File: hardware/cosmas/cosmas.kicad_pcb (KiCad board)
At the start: 2 copper layers, 23 parts, among them J1 12V DC, J2 I2C_LCD_SCREEN, J3 MOTORA, J4 MOTORB, J5 DRIVER-POWER, J6 MOTOR-CONTROL, J7 MOT_A, J8 MOT_A, SW1 ON/OFF, U2 AMS1117-3.3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

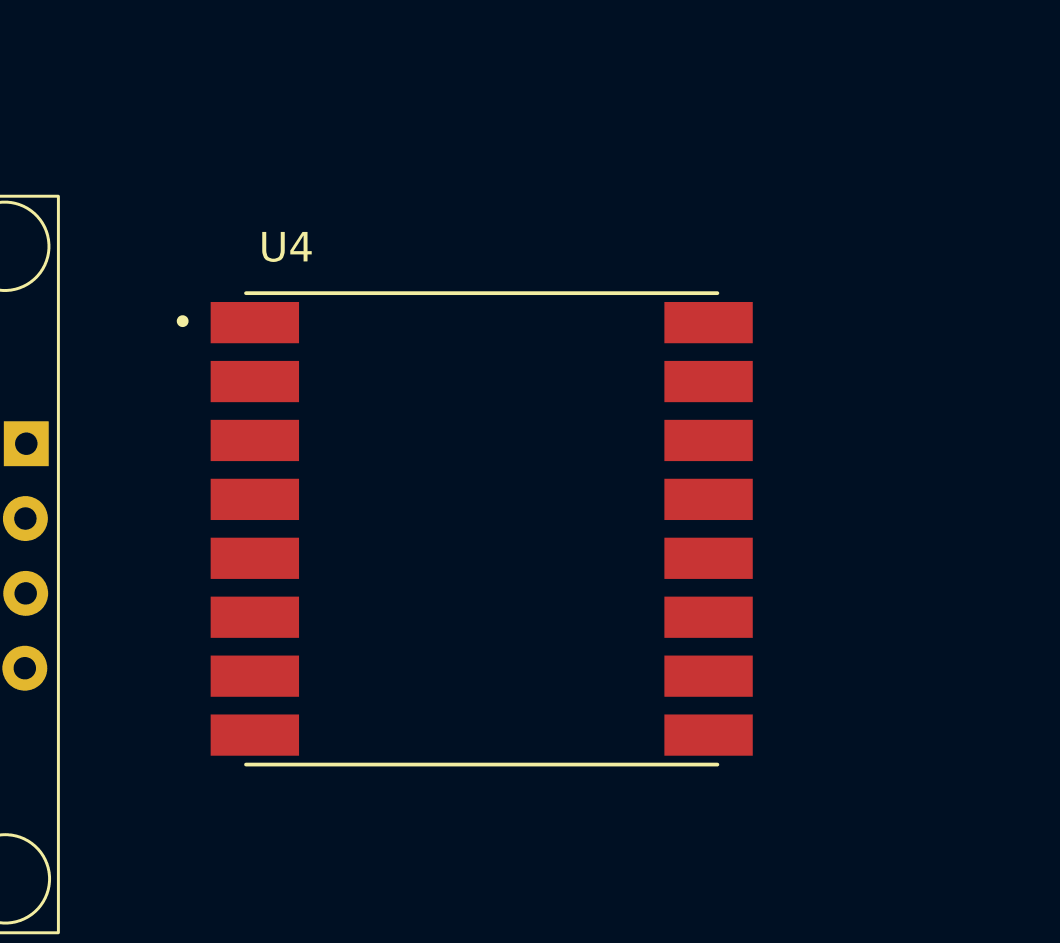
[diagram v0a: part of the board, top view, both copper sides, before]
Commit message: updates net labels
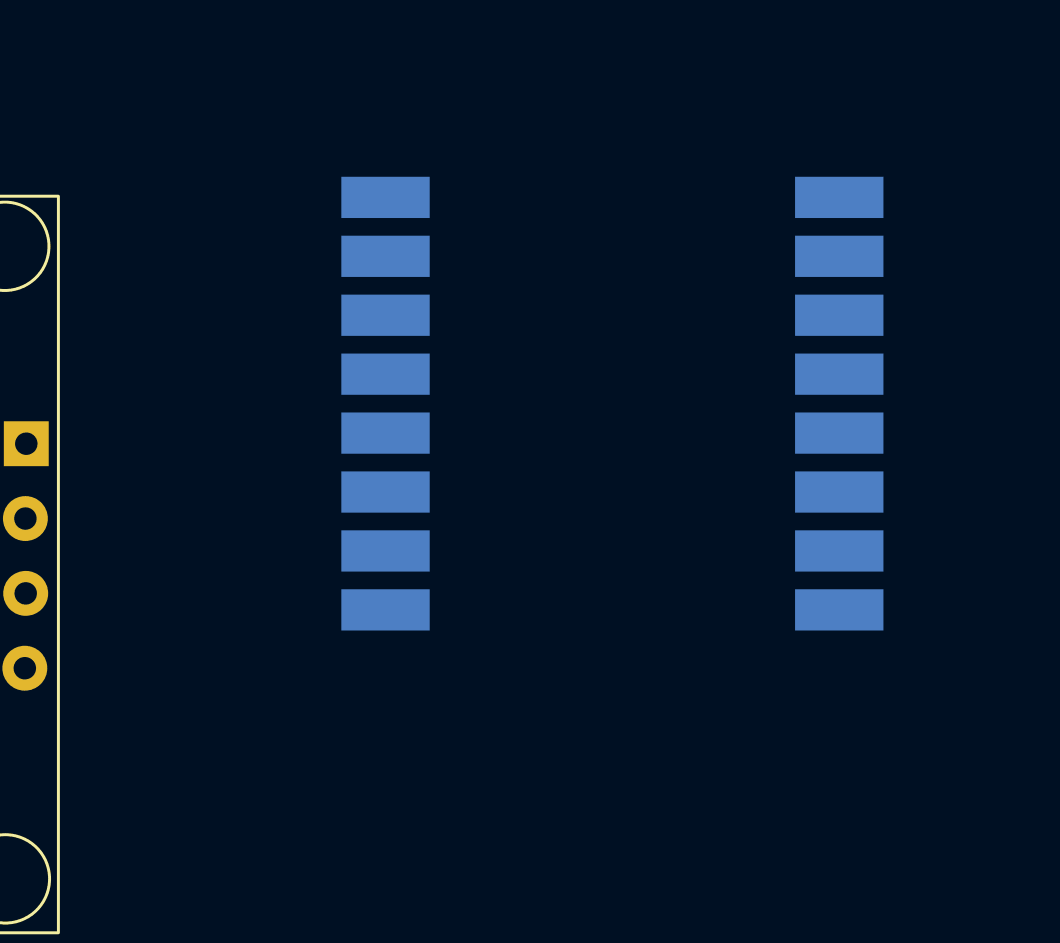
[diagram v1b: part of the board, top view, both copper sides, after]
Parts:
- U4: moved to B.Cu
- moved U4 6.14 mm to (84.0, 98.2), turned to 180 degrees
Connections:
- net /CPU/ENA renamed ENA
- net /CPU/ENB renamed ENB
- net /CPU/GPS_RX renamed GPX_RX
- net /CPU/IN1 renamed IN1
- net /CPU/IN2 renamed IN2
- net /CPU/IN3 renamed IN3
- net /CPU/IN4 renamed IN4
- net /CPU/SCL renamed SCL
- net /CPU/SDA renamed SDA
- net /GSM-LORA-GPS/BUZZER renamed BUZZER
- net /GSM-LORA-GPS/GPS_RX renamed GPS_RX
- net /GSM-LORA-GPS/GSM_4V renamed GSM_4V
- net /GSM-LORA-GPS/GSM_RST renamed GSM_RST
- U3 pad 1: /CPU/3V3 -> 3V3
- U3 pad 10: /CPU/MISO -> MISO
- U3 pad 15: /CPU/MOSI -> MOSI
- U3 pad 21: /CPU/DIO0 -> DIO0
- U3 pad 24: /CPU/GPS_TX -> GPS_TX
- U3 pad 25: /CPU/RST -> RST
- U3 pad 3: /CPU/CS -> CS
- U3 pad 6: /CPU/GSM_TX -> GSM_TX
- U3 pad 7: /CPU/GSM_RX -> GSM_RX
- U3 pad 9: /CPU/SCK -> SCK
- U4 pad 13: /GSM-LORA-GPS/3V3 -> 3V3
- U4 pad 14: /GSM-LORA-GPS/DIO0 -> DIO0
- U4 pad 2: /GSM-LORA-GPS/MISO -> MISO
- U4 pad 3: /GSM-LORA-GPS/MOSI -> MOSI
- U4 pad 4: /GSM-LORA-GPS/SCK -> SCK
- U4 pad 5: /GSM-LORA-GPS/CS -> CS
- U4 pad 6: /GSM-LORA-GPS/RST -> RST
- U5 pad 4: /GSM-LORA-GPS/GSM_RX -> GSM_RX
- U5 pad 5: /GSM-LORA-GPS/GSM_TX -> GSM_TX
- U6 pad 3: /GSM-LORA-GPS/GPS_TX -> GPS_TX

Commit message: adds OBC PCB
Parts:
- added C1: C_Small, Capacitor_THT:CP_Radial_D4.0mm_P2.00mm, F.Cu at (600.5, 34.2)
- U2: moved to B.Cu
- moved D1 616.9 mm to (606.4, -63.4)
- moved U1 610.0 mm to (629.6, 12.8), turned to 180 degrees
- moved R1 602.8 mm to (615.2, -19.3)
- moved SW1 600.8 mm to (613.9, -57.5), turned to -90 degrees
- moved J1 597.9 mm to (628.0, -53.5), turned to -90 degrees
- moved D2 588.0 mm to (627.8, -24.6)
- moved R3 576.9 mm to (597.6, 21.4), turned to 180 degrees
- moved U2 576.3 mm to (617.0, -41.4), turned to -90 degrees
- moved U7 574.5 mm to (614.5, -30.8)
- moved R2 562.4 mm to (582.5, 16.2)
- moved R4 562.2 mm to (582.4, 26.2)
- moved J8 530.8 mm to (602.7, -38.8)
- moved J6 496.5 mm to (576.6, -15.8), turned to 90 degrees
- moved U6 496.4 mm to (516.8, -6.75)
- moved J7 480.2 mm to (542.8, -39.2)
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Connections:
- net /power-supply/12V renamed 12V
- J2 pad 2: /Display/SCL -> SCL
- J2 pad 3: /Display/SDA -> SDA
- J2 pad 4: /Display/5V -> 5V
- J5 pad 1: /motors/6V -> 6V
- J5 pad 3: /motors/5V -> 5V
- J6 pad 1: /motors/ENA -> ENA
- J6 pad 2: /motors/ENB -> ENB
- J6 pad 3: /motors/IN1 -> IN1
- J6 pad 4: /motors/IN2 -> IN2
- J6 pad 5: /motors/IN3 -> IN3
- J6 pad 6: /motors/IN4 -> IN4
- R2 pad 1: /power-supply/6V -> 6V
- R3 pad 2: /power-supply/GSM_4V -> GSM_4V
- R4 pad 1: /power-supply/GSM_4V -> GSM_4V
- U1 pad 4: /power-supply/6V -> 6V
- U2 pad 2: /power-supply/3V3 -> 3V3
- U2 pad 3: /power-supply/5V -> 5V
- U3 pad 23: GPX_RX -> GPS_RX
- U3 pad 4: unconnected-(U3-D2-Pad4) -> BUZZER
- U4 pad 10: GND -> unconnected-(U4-GND-Pad10)
- U4 pad 8: GND -> unconnected-(U4-GND-Pad8)
- U6 pad 1: /GSM-LORA-GPS/5V -> 5V
- U7 pad 3: /power-supply/5V -> 5V
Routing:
- net GND: track 0.00 -> 396.7 mm, vias 0 -> 6
- net 3V3: track 0.00 -> 287.5 mm, vias 0 -> 2
- net 5V: track 0.00 -> 216.9 mm, vias 0 -> 4
- net IN3: track 0.00 -> 118.2 mm, vias 0 -> 2
- net IN2: track 0.00 -> 103.4 mm
- net GSM_RX: track 0.00 -> 99.7 mm, vias 0 -> 2
- net GSM_TX: track 0.00 -> 89.6 mm
- net Net-(J4-Pin_2): track 0.00 -> 87.6 mm
- net ENB: track 0.00 -> 87.2 mm
- net Net-(J4-Pin_1): track 0.00 -> 87.2 mm
- net IN4: track 0.00 -> 85.7 mm, vias 0 -> 2
- net IN1: track 0.00 -> 82.1 mm, vias 0 -> 2
- net ENA: track 0.00 -> 74.9 mm
- net SDA: track 0.00 -> 70.2 mm, vias 0 -> 2
- net 12V: track 0.00 -> 66.9 mm, vias 0 -> 2
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- added copper zone on B.Cu, net 12V
- added copper zone on B.Cu, net 3V3
- added copper zone on B.Cu, net 5V
- added copper zone on B.Cu, net Net-(D1-A)
- added copper zone on B.Cu, net Net-(SW1-A)
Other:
- board outline added: 120.3 x 185.9 mm

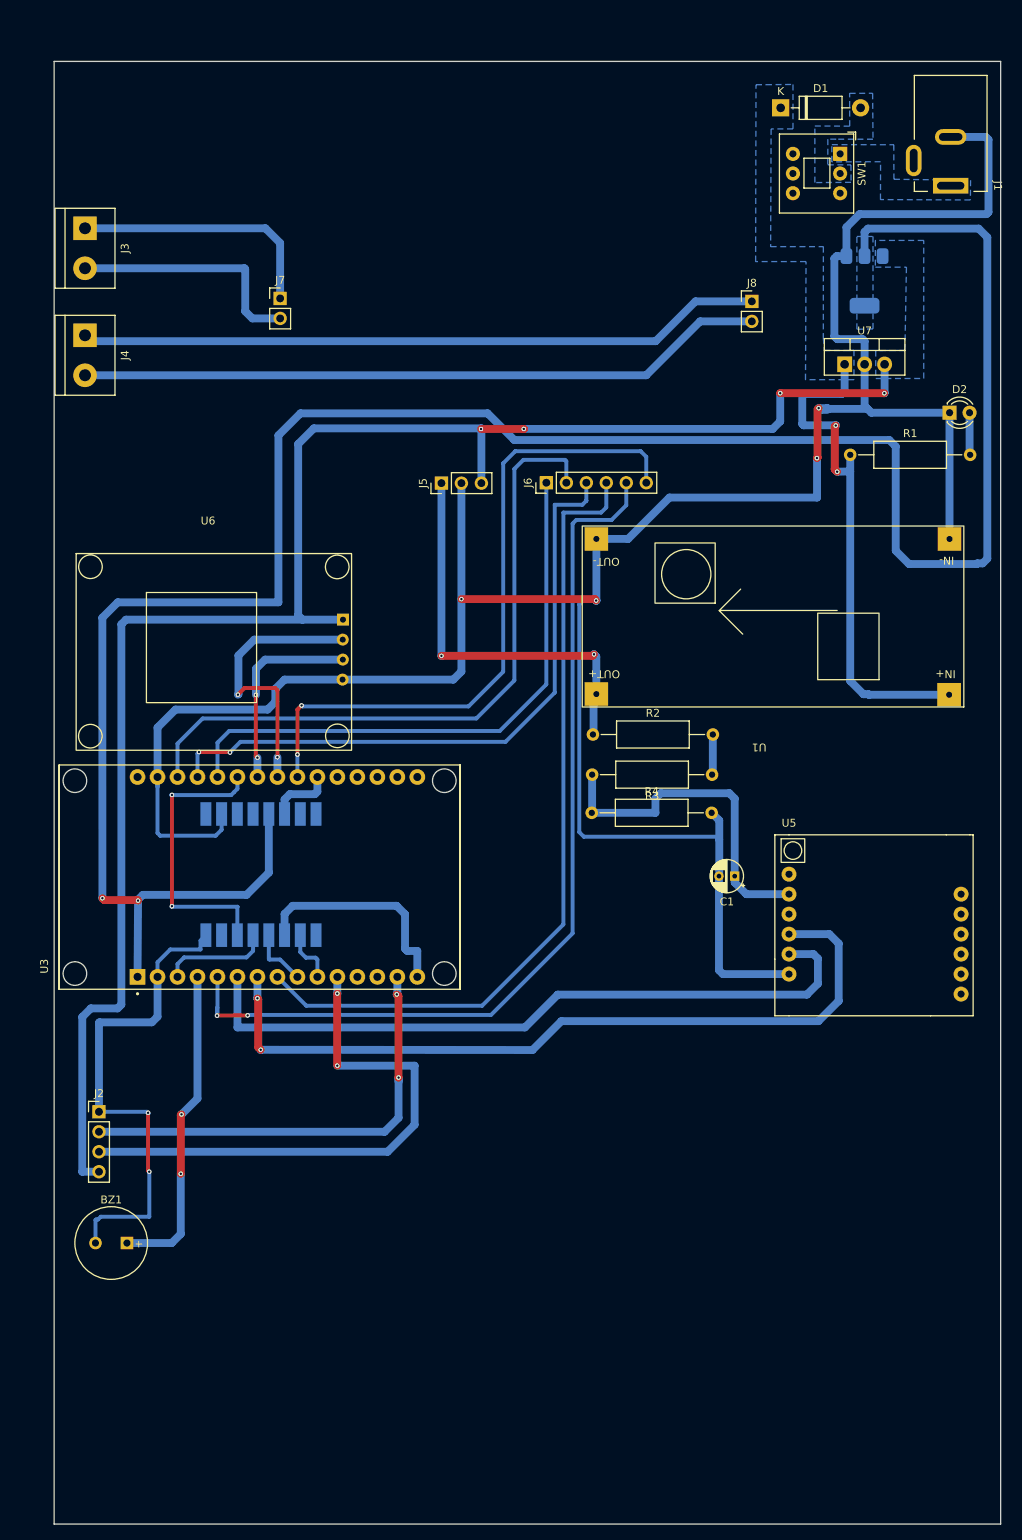
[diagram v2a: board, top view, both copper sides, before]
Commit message: adds lora TX
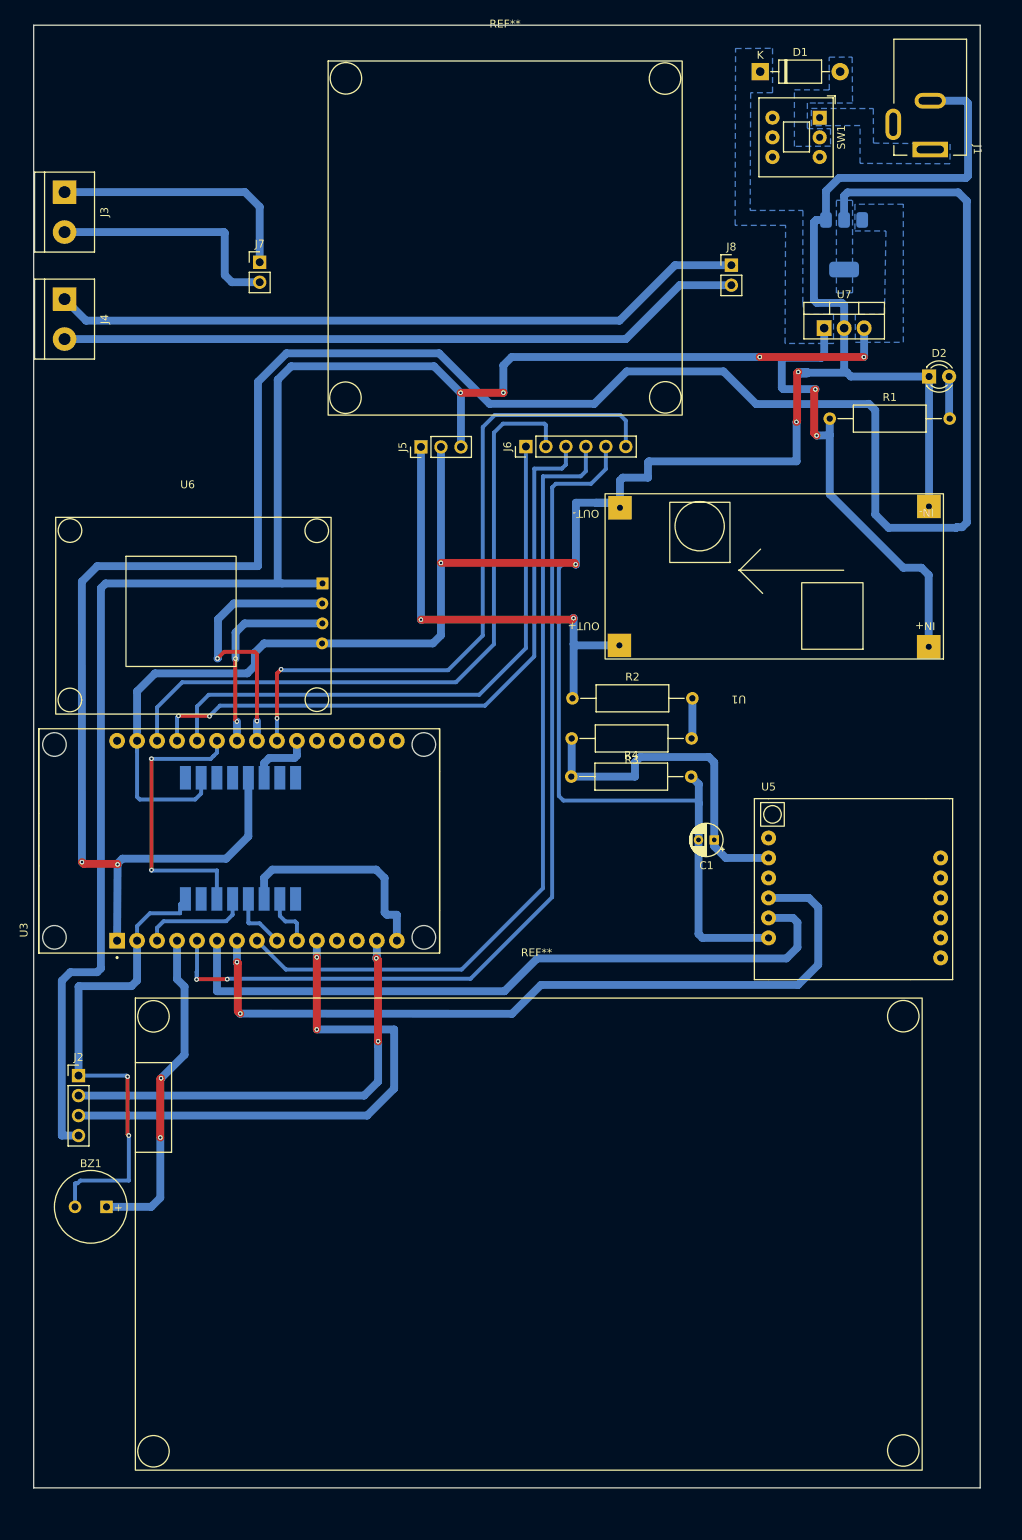
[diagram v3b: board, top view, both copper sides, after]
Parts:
- added REF**: I2C_LCD_20X4, my-modules:I2C_LCD_20X4, F.Cu at (524.4, 49.8)
- added REF**: L298N_MOTOR_DRIVER, my-modules:L298N_MOTOR_DRIVER, F.Cu at (548.9, -69.3)
- moved U1 6.63 mm to (627.0, 6.65)
- moved C1 5.28 mm to (597.9, 29.6)
- moved D1 5.28 mm to (603.8, -68.0)
- moved J1 5.28 mm to (625.4, -58.1)
- moved J2 5.28 mm to (517.1, 59.6)
- moved J4 5.28 mm to (515.4, -39.1)
- moved J5 5.28 mm to (560.6, -20.3)
- moved J7 5.28 mm to (540.1, -43.8)
- moved J8 5.28 mm to (600.1, -43.4)
- moved R3 5.28 mm to (595.0, 16.8)
- moved SW1 5.28 mm to (611.3, -62.1)
- moved U2 5.28 mm to (614.4, -46.0)
- moved U3 5.28 mm to (537.5, 29.8)
- moved U5 5.28 mm to (604.8, 29.4)
- moved R2 5.28 mm to (579.9, 11.7)
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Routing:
- net 3V3: track 287.5 -> 294.7 mm
- net 12V: track 66.9 -> 60.5 mm
- net 6V: track 52.0 -> 57.6 mm
- net GND: track 396.7 -> 402.3 mm
- net 5V: track 216.9 -> 220.7 mm
- net Net-(J4-Pin_1): track 87.2 -> 88.8 mm
- net BUZZER: track 40.9 -> 41.7 mm
